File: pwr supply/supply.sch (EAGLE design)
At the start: 5 parts

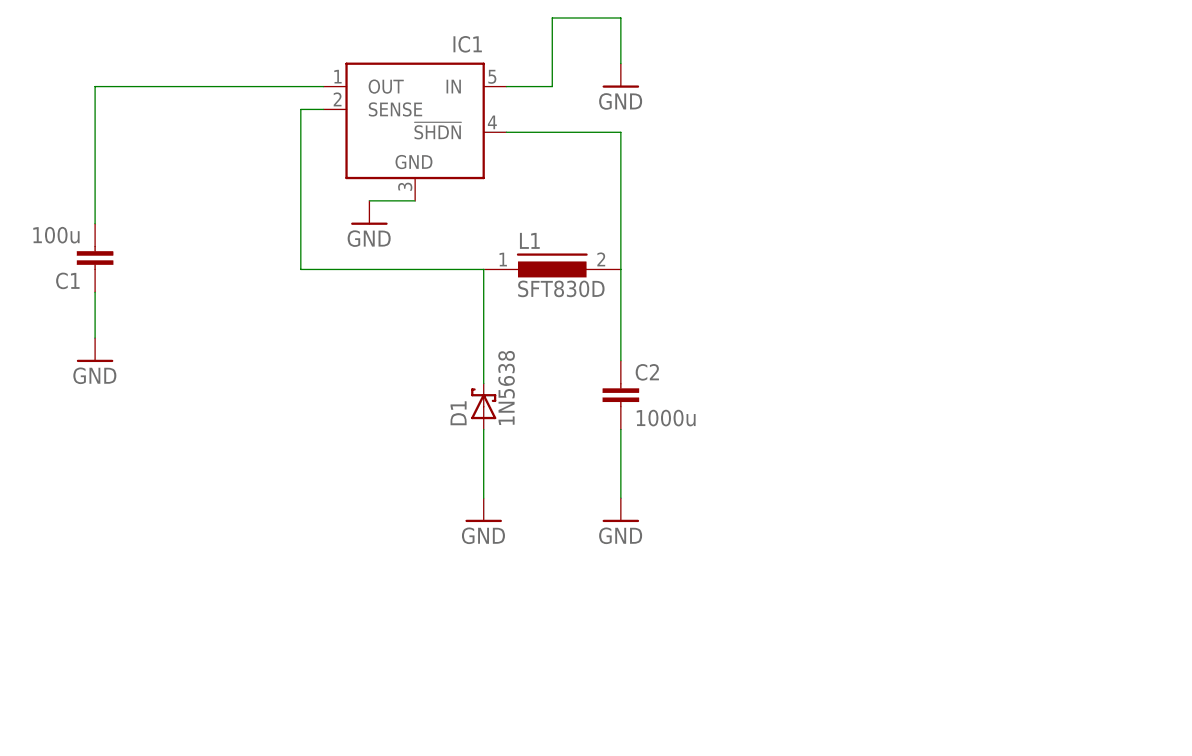
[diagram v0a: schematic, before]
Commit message: Added some bluetooth code
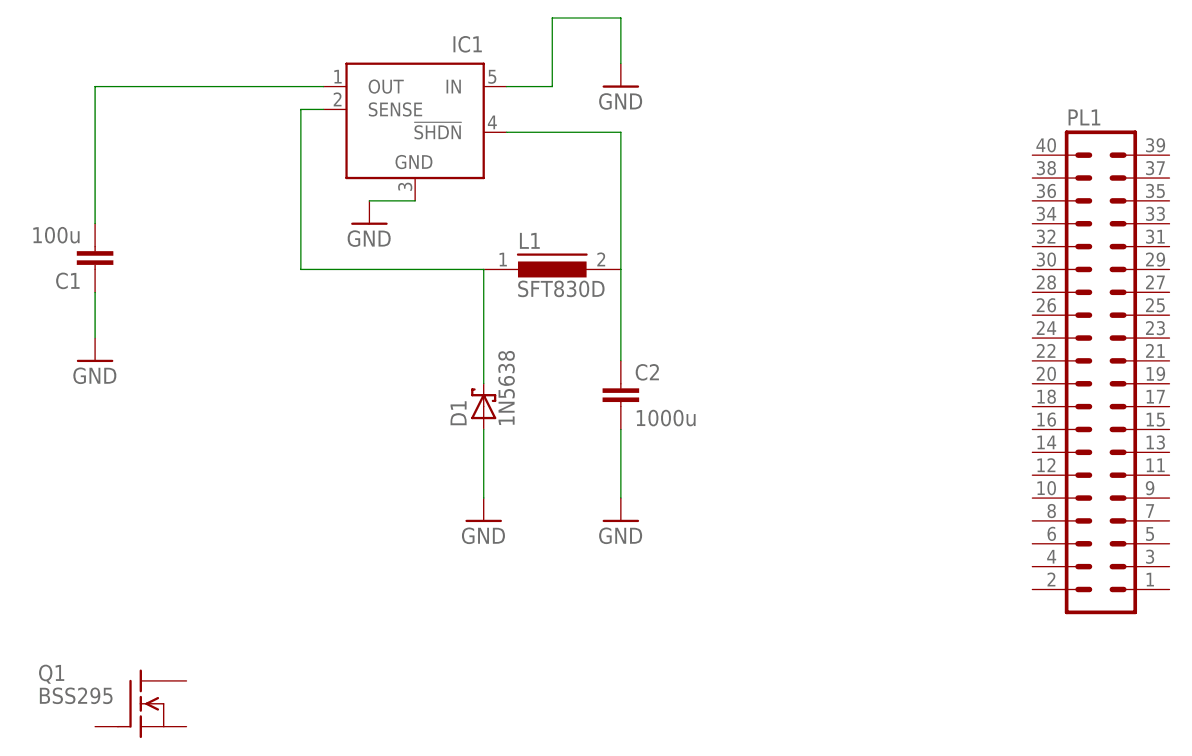
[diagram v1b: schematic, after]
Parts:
- added PL1: (no value), con-harting-v:40V
- added Q1: BSS295, transistor-fet:BSS295
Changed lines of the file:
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@@
 <?xml version="1.0" encoding="utf-8"?>
 <!DOCTYPE eagle SYSTEM "eagle.dtd">
-<eagle version="6.2">
+<eagle version="6.3">
 <drawing>
 <settings>
@@
 <part name="L1" library="inductors" deviceset="SFT830D" device=""/>
 <part name="GND5" library="supply1" deviceset="GND" device=""/>
+<part name="Q1" library="transistor-fet" deviceset="BSS295" device=""/>
+<part name="PL1" library="con-harting-v" deviceset="40V" device=""/>
 </parts>
 <sheets>
@@
 <instance part="L1" gate="G$1" x="78.74" y="40.64"/>
 <instance part="GND5" gate="1" x="86.36" y="60.96"/>
+<instance part="Q1" gate="G$1" x="33.02" y="-7.62"/>
+<instance part="PL1" gate="G$1" x="139.7" y="30.48"/>
 </instances>
 <busses>
